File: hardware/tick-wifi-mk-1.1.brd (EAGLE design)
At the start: 100 x 64 mm, 29 parts, among them IC1 MAX7219, IC2 MAX7219, IC3 74HC125, IC4 LD1117 5V

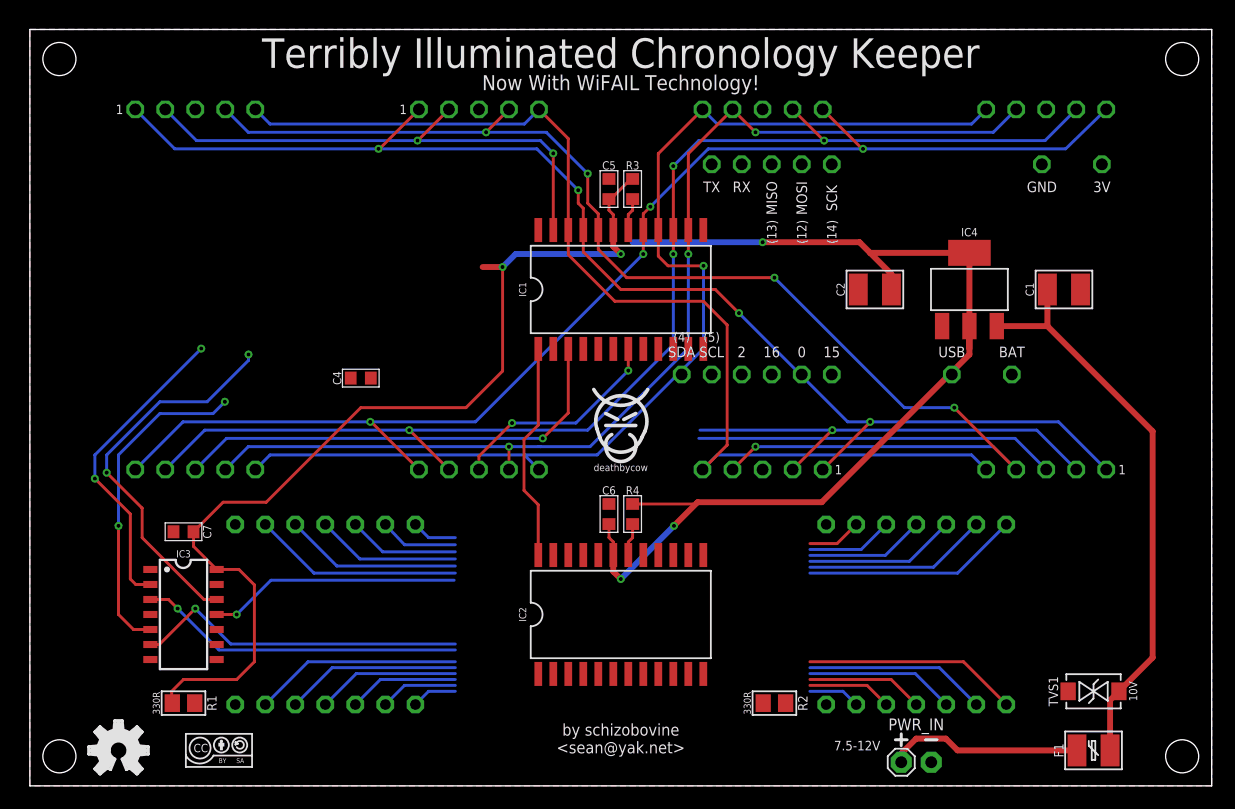
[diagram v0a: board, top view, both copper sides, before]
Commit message: layout finished for wifail board
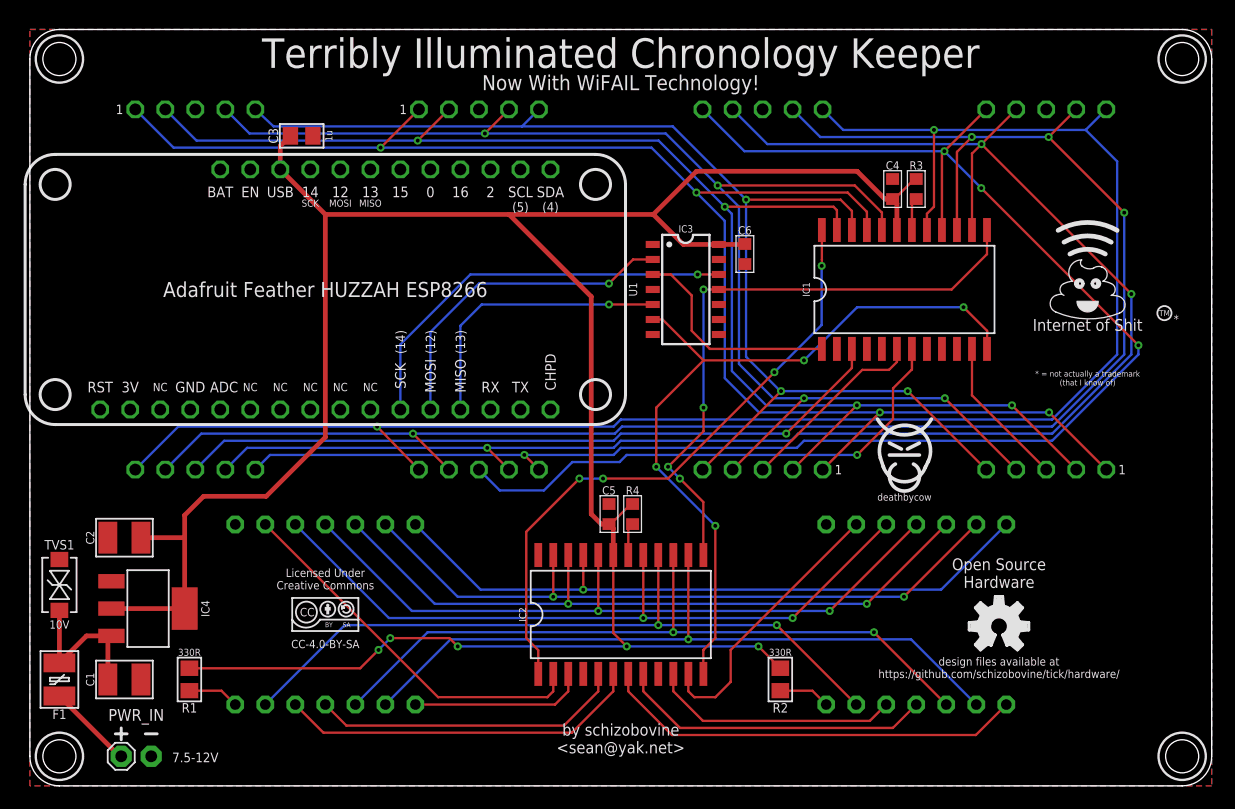
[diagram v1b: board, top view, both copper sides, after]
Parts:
- removed C7: 100n, a_parts:C0603
- added C3: 1u, a_parts:C0805
- added U$6: (no value), A_butts:CC-BY-SA-4.0-NO-URL
- added U$7, U$8: (no value), a_parts:INTERNET_OF_SHIT
- added U1: Adafruit Feather HUZZAH ESP8266, a_parts:ADAFRUIT_FEATHER_HUZZAH
- U$5: value ADAFRUIT_FEATHER_HUZZAH_ESP8266_TICK -> (none); device a_parts:ADAFRUIT_FEATHER_HUZZAH_TICK -> a_parts:OSHWLOGO_TINY_SILKONLY
- moved TVS1 88.0 mm to (2.50, 17.0), turned to 270 degrees
- moved F1 87.7 mm to (2.50, 9.00), turned to 90 degrees
- moved C1 86.1 mm to (8.00, 9.00)
- moved U$3 75.2 mm to (82.0, 13.5)
- moved IC4 74.6 mm to (10.0, 15.0), turned to 270 degrees
- moved C2 66.9 mm to (8.00, 21.0)
- moved PWR_IN 66.0 mm to (9.00, 2.50)
- moved IC3 50.6 mm to (55.5, 42.0)
- moved C4 47.8 mm to (73.0, 50.5), turned to 270 degrees
- moved U$5 43.3 mm to (87.5, 2.50), flipped to the bottom, turned to 0 degrees
- moved C5 27.5 mm to (49.0, 23.0)
- moved C6 24.8 mm to (60.5, 45.0)
- moved U$2 24.1 mm to (74.0, 28.5)
- moved IC1 24.0 mm to (74.0, 42.0)
- moved R3 24.0 mm to (75.0, 50.5)
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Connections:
- removed net 3.3V: U$5.3V
- removed net N$7: IC1.10
- removed net N$8: IC1.5
- removed net N$9: IC1.8
- removed net SCL: U$5.SCL
- removed net SDA: U$5.SDA
- net 5V: now also C3.1, C4.2, C6.1, U1.USB; no longer C6.2, C7.1, U$5.USB
- net CTRL_CLCK: now also U1.SCK; no longer U$5.SCK
- net CTRL_DATA: now also U1.MOSI; no longer U$5.MOSI
- net CTRL_LOAD: now also U1.MISO; no longer U$5.MISO
- net DIG_10: now also IC2.8; no longer IC2.10
- net DIG_11: now also IC2.10; no longer IC2.5
- net DIG_12: now also IC2.11; no longer IC2.8
- net DIG_5: now also IC2.3; no longer IC2.2
- net DIG_6: now also IC2.5; no longer IC2.11
- net DIG_8: now also IC2.2; no longer IC2.7
- net DIG_9: now also IC2.7; no longer IC2.3
- net DISP_DATA: now also IC1.1; no longer IC2.1
- net DOUT1_DIN2: now also IC1.24, IC2.1; no longer IC1.1, IC2.24
- net GND: now also C3.2, C4.1, C6.2, U1.GND@0; no longer C6.1, C7.2, U$5.GND@0
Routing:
- net SEG_1A: track 92.7 -> 140.4 mm
- net 5V: track 175.0 -> 220.5 mm
- net SEG_1B: track 94.1 -> 138.2 mm, vias 1 -> 4
- net SEG_2A: track 22.0 -> 61.7 mm, vias 0 -> 1
- net SEG_2F: track 22.0 -> 61.6 mm, vias 0 -> 2
- net SEG_2G: track 22.3 -> 61.9 mm, vias 0 -> 2
- net SEG_2B: track 22.0 -> 61.5 mm, vias 0 -> 2
- net SEG_1G: track 107.3 -> 146.5 mm, vias 4 -> 2
- net SEG_2C: track 22.3 -> 60.8 mm, vias 0 -> 2
- net SEG_1F: track 107.0 -> 144.9 mm
- net SEG_1D: track 82.6 -> 120.2 mm, vias 3 -> 4
- net SEG_2P: track 22.3 -> 59.7 mm, vias 0 -> 2
- net SEG_2D: track 22.2 -> 58.6 mm, vias 0 -> 2
- net DISP_LOAD: track 28.3 -> 64.6 mm, vias 1 -> 4
- net SEG_2E: track 22.2 -> 57.5 mm, vias 0 -> 1
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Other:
- outline, holes or cut-outs redrawn
- board text added: "*"
- board text added: "* = not actually a trademark (that I know of)"
- board text added: "CC-4.0-BY-SA"
- board text added: "Internet of Shit"
- board text added: "Licensed Under Creative Commons"
- board text added: "Open Source Hardware"
- board text added: "TM"
- board text added: "design files available at https://github.com/schizobovine/tick/hardware/"

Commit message: more wip
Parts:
- removed C3: 1u, a_parts:C0805
- removed C4: 100n, a_parts:C0603
- removed PWR_IN: M02PTH-CENTERED-R+, A_butts:1X02-CENTER-R+
- removed U$5: (no value), a_parts:OSHWLOGO_TINY_SILKONLY
- removed U$6: (no value), A_butts:CC-BY-SA-4.0-NO-URL
- removed U$7, U$8: (no value), a_parts:INTERNET_OF_SHIT
- added C7: 100n, a_parts:C0603
- added PWR1: DCBARRELPTH, a_parts:DCJACK_2MM_PTH
- DIGIT1, DIGIT2, DIGIT3, DIGIT4: device A_butts:7SEG_1DIG_25.4MM_NOSILK -> a_parts:7SEG_1DIG_25.4MM_NOSILK
- DISPLAY1, DISPLAY2: value 7SEG_4DIGIT_COLON14.2MM-CC -> 7SEG_4DIGIT_COLON_APOS; device a_parts:7SEG_4DIG_0.56IN_14MM_ADAFRUIT -> a_parts:7SEG_4DIG_10MM
- F1: device A_butts:PTC-1210 -> a_parts:PTC-1210
- FRAME1: device A_butts:DUMMY -> a_parts:DUMMY
- TVS1: device A_butts:SMA-DIODE-TVS-BIDIR -> a_parts:SMA-DIODE-TVS-BIDIR
- U$1: device A_butts:TICK_SYMBOL -> a_parts:TICK_SYMBOL
- U$2: device A_butts:COW_SMALL -> a_parts:COW_SMALL
- U$4: device A_butts:CC-BY-SA-4.0-NO-URL -> a_parts:CC-BY-SA-4.0-NO-URL
- U1: value Adafruit Feather HUZZAH ESP8266 -> ADAFRUIT_FEATHER_HUZZAH_ESP8266_TICK; device a_parts:ADAFRUIT_FEATHER_HUZZAH -> a_parts:ADAFRUIT_FEATHER_HUZZAH_TICK
- moved U$4 74.2 mm to (93.5, 43.0), turned to 90 degrees
- moved U1 56.5 mm to (79.0, 25.4), turned to 90 degrees
- moved U$2 50.8 mm to (24.0, 37.5)
- moved C6 31.1 mm to (47.0, 17.0)
- moved IC3 28.7 mm to (79.0, 25.6), turned to 180 degrees
- moved IC1 27.8 mm to (48.0, 32.1)
- moved R3 27.5 mm to (49.0, 41.5)
- moved U$3 25.3 mm to (93.5, 36.0), turned to 90 degrees
- moved TVS1 19.5 mm to (3.00, 36.5)
- moved F1 19.0 mm to (3.00, 28.0)
- moved C5 18.6 mm to (47.0, 41.5)
- moved C2 17.6 mm to (10.0, 38.5)
- moved IC4 17.0 mm to (10.0, 32.0)
- moved C1 16.6 mm to (10.0, 25.5)
- moved R1 14.8 mm to (24.4, 19.0), turned to 180 degrees
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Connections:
- net 5V: now also C6.2, C7.1; no longer C3.1, C4.2, C6.1
- net DIG_10: now also DISPLAY2.2, IC2.10; no longer DISPLAY2.P$11, IC2.8
- net DIG_11: now also DISPLAY2.6, IC2.5; no longer DISPLAY2.P$10, IC2.10
- net DIG_12: now also DISPLAY2.8, IC2.8; no longer DISPLAY2.P$6, IC2.11
- net DIG_5: now also DISPLAY1.1, IC2.2; no longer DISPLAY1.P$14, IC2.3
- net DIG_6: now also DISPLAY1.2, IC2.11; no longer DISPLAY1.P$11, IC2.5
- net DIG_7: now also DISPLAY1.6; no longer DISPLAY1.P$10
- net DIG_8: now also DISPLAY1.8, IC2.7; no longer DISPLAY1.P$6, IC2.2
- net DIG_9: now also DISPLAY2.1, IC2.3; no longer DISPLAY2.P$14, IC2.7
- net GND: now also C6.1, C7.2, DISPLAY1.12, DISPLAY2.12, PWR1.BRK; no longer C3.2, C4.1, C6.2, DISPLAY1.P$7, DISPLAY2.P$7, PWR_IN.1
- net N$1: now also PWR1.PWR; no longer PWR_IN.2
- net N$3: now also DISPLAY1.4; no longer DISPLAY1.P$8
- net N$5: now also DISPLAY2.4; no longer DISPLAY2.P$8
- net SEG_2A: now also DISPLAY1.14, DISPLAY2.14; no longer DISPLAY1.P$13, DISPLAY2.P$13
- net SEG_2B: now also DISPLAY1.16, DISPLAY2.16; no longer DISPLAY1.P$9, DISPLAY2.P$9
- net SEG_2C: now also DISPLAY1.13, DISPLAY2.13; no longer DISPLAY1.P$4, DISPLAY2.P$4
- net SEG_2D: now also DISPLAY1.3, DISPLAY2.3; no longer DISPLAY1.P$2, DISPLAY2.P$2
- net SEG_2E: now also DISPLAY1.5, DISPLAY2.5; no longer DISPLAY1.P$1, DISPLAY2.P$1
- net SEG_2F: now also DISPLAY1.11, DISPLAY2.11; no longer DISPLAY1.P$12, DISPLAY2.P$12
- net SEG_2G: now also DISPLAY1.15, DISPLAY2.15; no longer DISPLAY1.P$5, DISPLAY2.P$5
- net SEG_2P: now also DISPLAY1.7, DISPLAY2.7; no longer DISPLAY1.P$3, DISPLAY2.P$3
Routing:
- net 5V: track 220.5 -> 0.00 mm, vias 5 -> 0
- net SEG_1G: track 146.5 -> 0.00 mm, vias 2 -> 0
- net SEG_1F: track 144.9 -> 0.00 mm, vias 4 -> 0
- net SEG_1A: track 140.4 -> 0.00 mm, vias 3 -> 0
- net SEG_1B: track 138.2 -> 0.00 mm, vias 4 -> 0
- net SEG_1E: track 130.6 -> 0.00 mm, vias 4 -> 0
- net SEG_1D: track 120.2 -> 0.00 mm, vias 4 -> 0
- net SEG_1C: track 115.1 -> 0.00 mm, vias 4 -> 0
- net SEG_1P: track 104.6 -> 0.00 mm, vias 3 -> 0
- net DISP_LOAD: track 64.6 -> 0.00 mm, vias 4 -> 0
- net SEG_2G: track 61.9 -> 0.00 mm, vias 2 -> 0
- net SEG_2A: track 61.7 -> 0.00 mm, vias 1 -> 0
- net SEG_2F: track 61.6 -> 0.00 mm, vias 2 -> 0
- net SEG_2B: track 61.5 -> 0.00 mm, vias 2 -> 0
- net SEG_2C: track 60.8 -> 0.00 mm, vias 2 -> 0
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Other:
- board size 100 x 64 mm -> 96 x 54 mm
- board text removed: "*"
- board text removed: "* = not actually a trademark (that I know of)"
- board text removed: "CC-4.0-BY-SA"
- board text removed: "Internet of Shit"
- board text removed: "Licensed Under Creative Commons"
- board text removed: "Open Source Hardware"
- board text removed: "TM"
- board text removed: "design files available at https://github.com/schizobovine/tick/hardware/"

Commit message: more wip again
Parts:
- removed U1: ADAFRUIT_FEATHER_HUZZAH_ESP8266_TICK, a_parts:ADAFRUIT_FEATHER_HUZZAH_TICK
- added JP1: M05PTH-CENTERED, a_parts:1X05_PTH_CENTERED
- moved U$4 40.4 mm to (88.0, 3.00), turned to 0 degrees
- moved U$3 35.1 mm to (81.5, 3.00), turned to 0 degrees
- moved C7 16.4 mm to (88.0, 36.0), turned to 270 degrees
- moved IC3 7.34 mm to (82.6, 32.0), turned to 270 degrees
- moved IC1 0.10 mm to (48.0, 32.0)
- moved U$1 0.10 mm to (48.0, 32.0)
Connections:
- net 5V: now also JP1.5; no longer U1.USB
- net CTRL_CLCK: now also JP1.3; no longer U1.SCK
- net CTRL_DATA: now also JP1.2; no longer U1.MOSI
- net CTRL_LOAD: now also JP1.1; no longer U1.MISO
- net DIG_2: now also IC1.7; no longer IC1.6
- net DIG_3: now also IC1.6; no longer IC1.7
- net DIG_4: now also IC1.2; no longer IC1.3
- net GND: now also JP1.4; no longer U1.GND@0

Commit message: wip
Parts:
- R1, R2: device a_parts:R0805 -> a_parts:R0603
- moved R2 12.8 mm to (69.9, 17.8), turned to 90 degrees
- moved R1 2.28 mm to (23.3, 17.0), turned to 90 degrees
- moved C5 0.50 mm to (46.5, 41.5)
- moved C6 0.50 mm to (46.5, 17.0)
- moved R3 0.50 mm to (49.5, 41.5)
- moved R4 0.50 mm to (49.5, 17.0)
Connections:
- net DIG_1: now also IC1.2; no longer IC1.11
- net DIG_2: now also IC1.11; no longer IC1.7
- net DIG_4: now also IC1.7; no longer IC1.2
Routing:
- net 5V: track 0.00 -> 148.5 mm, vias 0 -> 3
- net SEG_1G: track 0.00 -> 131.1 mm, vias 0 -> 5
- net SEG_1E: track 0.00 -> 131.1 mm, vias 0 -> 6
- net SEG_1D: track 0.00 -> 123.8 mm, vias 0 -> 7
- net SEG_1F: track 0.00 -> 123.8 mm, vias 0 -> 5
- net SEG_1C: track 0.00 -> 113.0 mm, vias 0 -> 6
- net SEG_1A: track 0.00 -> 113.0 mm, vias 0 -> 5
- net SEG_1P: track 0.00 -> 108.9 mm, vias 0 -> 7
- net SEG_1B: track 0.00 -> 108.9 mm, vias 0 -> 5
- net DISP_CLCK: track 0.00 -> 81.7 mm, vias 0 -> 3
- net DISP_LOAD: track 0.00 -> 55.5 mm, vias 0 -> 3
- net SEG_2D: track 0.00 -> 50.4 mm, vias 0 -> 2
- net SEG_2E: track 0.00 -> 50.3 mm, vias 0 -> 2
- net SEG_2P: track 0.00 -> 50.0 mm, vias 0 -> 2
- net DIG_1: track 0.00 -> 48.4 mm, vias 0 -> 2
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
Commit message: new tick version
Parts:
- removed PWR1: DCBARRELPTH, a_parts:DCJACK_2MM_PTH
- added JP2: M02PTH-CENTERED-R+, a_parts:1X02-CENTER-R+
- added U$10: (no value), a_parts:F_YOU_MARK_METAL
- added U$5: (no value), A_butts:COW_SMALL
- added U$6: (no value), A_butts:CC-BY-SA-4.0-NO-URL
- added U$7: (no value), a_parts:OSHWLOGO_SILKONLY
- added U$8: (no value), a_parts:INTERNET_OF_SHIT_JR_METAL
- added U$9: (no value), a_parts:COW_SMALL_METAL_NOTEXT
- U$3: device a_parts:OSHWLOGO_SILKONLY -> a_parts:INTERNET_OF_SHIT_TEXT_METAL
- U$4: device a_parts:CC-BY-SA-4.0-NO-URL -> a_parts:INTERNET_OF_SHIT_TEXT
- moved U$4 79.2 mm to (9.00, 8.50)
- moved U$3 72.7 mm to (9.00, 8.50)
- moved TVS1 12.7 mm to (11.5, 27.0), turned to 90 degrees
- moved R2 12.5 mm to (77.0, 7.50)
- moved R1 10.4 mm to (19.0, 7.50)
- moved C1 5.66 mm to (6.00, 29.5), turned to 180 degrees
- moved C2 5.66 mm to (6.00, 42.5)
- moved IC4 5.66 mm to (6.00, 36.0)
- moved F1 4.61 mm to (6.00, 24.5), turned to 0 degrees
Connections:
- net GND: now also JP2.1; no longer PWR1.BRK
- net N$1: now also JP2.2; no longer PWR1.PWR
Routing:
- net 5V: track 148.5 -> 227.0 mm, vias 3 -> 5
- net N$5: track 0.00 -> 23.0 mm, vias 0 -> 2
- net VIN: track 0.00 -> 16.7 mm
- net N$3: track 0.00 -> 11.5 mm
- net N$1: track 0.00 -> 4.31 mm
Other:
- outline, holes or cut-outs redrawn
- board text added: "5V"
- board text added: "C"
- board text added: "CC-4.0-BY-SA"
- board text added: "CLK"
- board text added: "DAT"
- board text added: "DC IN 7-12V"
- board text added: "GND"
- board text added: "I"
- board text added: "Internet of Shit"
- board text added: "K"
- board text added: "LD"
- board text added: "Licensed Under Creative Commons"
- board text added: "Open Source Hardware"
- board text added: "T"
- board text added: "design files available at https://github.com/schizobovine/tick/hardware/"
- board text added: "eeper"
- board text added: "erribly"
- board text added: "hronology"
- board text added: "lluminated"
- board text removed: "7.5-12V"
